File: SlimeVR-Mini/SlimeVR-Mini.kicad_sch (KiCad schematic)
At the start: 1 part, among them U1 ESP32-C3-MINI-1-N4

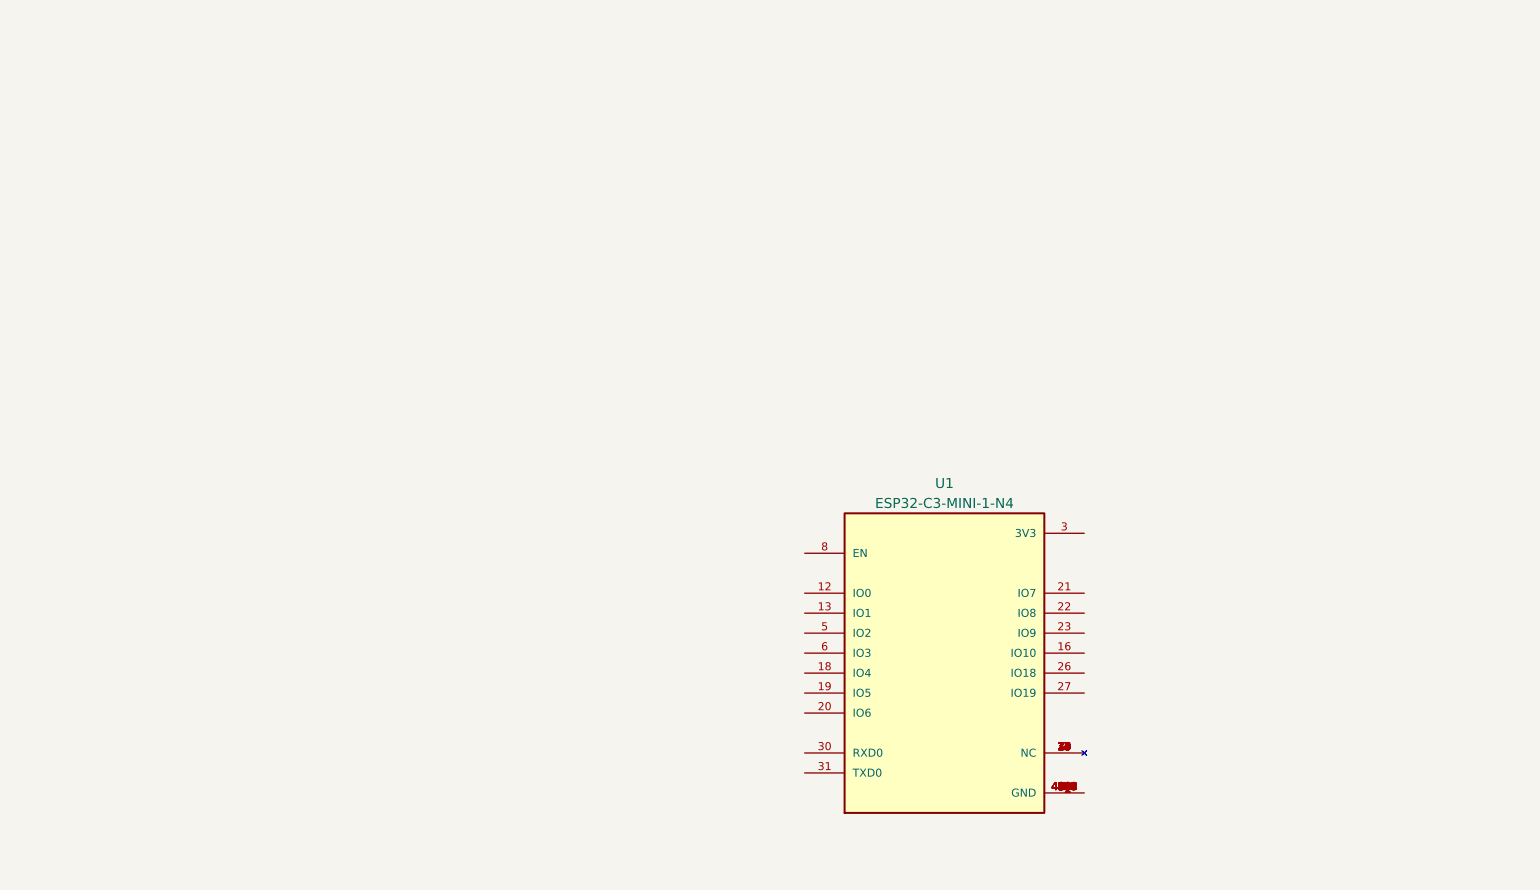
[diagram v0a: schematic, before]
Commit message: basic sheet hierarchy + schematic todo list
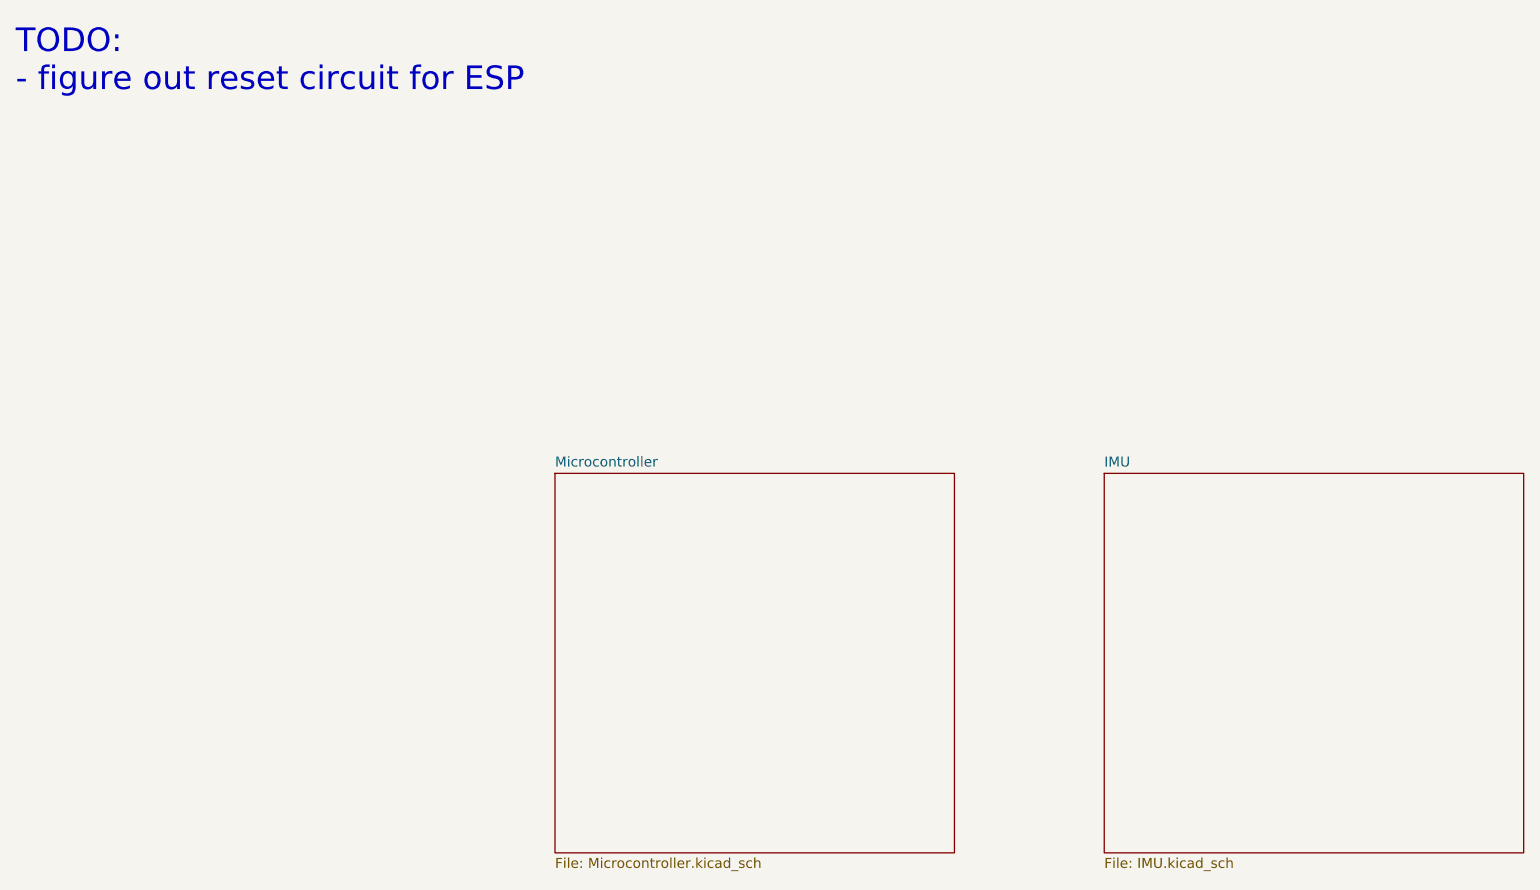
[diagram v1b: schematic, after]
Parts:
- removed U1: ESP32-C3-MINI-1-N4, Project Library:XCVR_ESP32-C3-MINI-1-N4, symbol Project Library:ESP32-C3-MINI-1-N4
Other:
- added sheet IMU (IMU.kicad_sch)
- added sheet Microcontroller (Microcontroller.kicad_sch)
- note added: "TODO: - figure out reset circuit for ESP"
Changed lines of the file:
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@@
 (kicad_sch (version 20230121) (generator eeschema)
   (paper "A4")
-  (symbol (lib_id "Project Library:ESP32-C3-MINI-1-N4") (at 132.08 95.25 0) (unit 1)
-    (in_bom yes) (on_board yes) (dnp no) (fields_autoplaced)
-    (property "Reference" "U1" (at 132.08 73.66 0)
-      (effects (font (size 1.27 1.27)))
+  (text "TODO:\n- figure out reset circuit for ESP\n" (at 13.97 24.13 0)
+    (effects (font (size 3 3)) (justify left bottom))
+  )
+  (sheet (at 152.4 72.39) (size 53.34 48.26) (fields_autoplaced)
+    (stroke (width 0.1524) (type solid))
+    (fill (color 0 0 0 0.0000))
+    (property "Sheetname" "IMU" (at 152.4 71.6784 0)
+      (effects (font (size 1.27 1.27)) (justify left bottom))
     )
-    (property "Value" "ESP32-C3-MINI-1-N4" (at 132.08 76.2 0)
-      (effects (font (size 1.27 1.27)))
+    (property "Sheetfile" "IMU.kicad_sch" (at 152.4 121.2346 0)
+      (effects (font (size 1.27 1.27)) (justify left top))
     )
-    (property "Footprint" "Project Library:XCVR_ESP32-C3-MINI-1-N4" (at 132.08 95.25 0)
-      (effects (font (size 1.27 1.27)) (justify bottom) hide)
-    )
-    (property "Datasheet" "https://www.espressif.com/sites/default/files/documentation/esp32-c3-mini-1_datasheet_en.pdf" (at 132.08 120.65 0)
-      (effects (font (size 1.27 1.27)) hide)
-    )
-    (property "MF" "Espressif Systems" (at 132.08 95.25 0)
-      (effects (font (size 1.27 1.27)) (justify bottom) hide)
-    )
-    (property "MAXIMUM_PACKAGE_HEIGHT" "2.55mm" (at 132.08 95.25 0)
-      (effects (font (size 1.27 1.27)) (justify bottom) hide)
-    )
-    (property "Package" "SMD-53 Espressif Systems" (at 132.08 95.25 0)
-      (effects (font (size 1.27 1.27)) (justify bottom) hide)
-    )
-    (property "PARTREV" "v1.0" (at 132.08 95.25 0)
-      (effects (font (size 1.27 1.27)) (justify bottom) hide)
-    )
-    (property "MP" "ESP32-C3-MINI-1-N4" (at 132.08 95.25 0)
-      (effects (font (size 1.27 1.27)) (justify bottom) hide)
-    )
-    (property "MANUFACTURER" "Espressif Systems" (at 132.08 95.25 0)
-      (effects (font (size 1.27 1.27)) (justify bottom) hide)
-    )
-    (pin "1")
-    (pin "10")
-    (pin "11")
-    (pin "12")
-    (pin "13")
-    (pin "14")
-    (pin "15")
-    (pin "16")
-    (pin "17")
-    (pin "18")
-    (pin "19")
-    (pin "2")
-    (pin "20")
-    (pin "21")
-    (pin "22")
-    (pin "23")
-    (pin "24")
-    (pin "25")
-    (pin "26")
-    (pin "27")
-    (pin "28")
-    (pin "29")
-    (pin "3")
-    (pin "30")
-    (pin "31")
-    (pin "32")
-    (pin "33")
-    (pin "34")
-    (pin "35")
-    (pin "36")
-    (pin "37")
-    (pin "38")
-    (pin "39")
-    (pin "4")
-    (pin "40")
-    (pin "41")
-    (pin "42")
-    (pin "43")
-    (pin "44")
-    (pin "45")
-    (pin "46")
-    (pin "47")
-    (pin "48")
-    (pin "49_1")
-    (pin "49_2")
-    (pin "49_3")
-    (pin "49_4")
-    (pin "49_5")
-    (pin "49_6")
-    (pin "49_7")
-    (pin "49_8")
-    (pin "49_9")
-    (pin "5")
-    (pin "50")
-    (pin "51")
-    (pin "52")
-    (pin "53")
-    (pin "6")
-    (pin "7")
-    (pin "8")
-    (pin "9")
     (instances
       (project "SlimeVR-Mini"
-        (path "/01f70e2f-47c6-495b-b6f7-eee456c9fb57"
-          (reference "U1") (unit 1)
-        )
+        (path "/01f70e2f-47c6-495b-b6f7-eee456c9fb57" (page "3"))
       )
     )
+  )
+  (sheet (at 82.55 72.39) (size 50.8 48.26) (fields_autoplaced)
+    (stroke (width 0.1524) (type solid))
+    (fill (color 0 0 0 0.0000))
+    (property "Sheetname" "Microcontroller" (at 82.55 71.6784 0)
+      (effects (font (size 1.27 1.27)) (justify left bottom))
+    )
+    (property "Sheetfile" "Microcontroller.kicad_sch" (at 82.55 121.2346 0)
+      (effects (font (size 1.27 1.27)) (justify left top))
+    )
+    (instances
+      (project "SlimeVR-Mini"
+        (path "/01f70e2f-47c6-495b-b6f7-eee456c9fb57" (page "2"))
+      )
+    )

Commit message: IMU wiring done-ish
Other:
- sheet IMU ports: added SCL, SDA; removed none
- sheet Microcontroller ports: added SCL, SDA; removed none
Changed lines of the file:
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@@
     (effects (font (size 3 3)) (justify left bottom))
   )
-  (sheet (at 152.4 72.39) (size 53.34 48.26) (fields_autoplaced)
+  (sheet (at 152.4 95.25) (size 17.78 12.7) (fields_autoplaced)
     (stroke (width 0.1524) (type solid))
     (fill (color 0 0 0 0.0000))
-    (property "Sheetname" "IMU" (at 152.4 71.6784 0)
+    (property "Sheetname" "IMU" (at 152.4 94.5384 0)
       (effects (font (size 1.27 1.27)) (justify left bottom))
     )
-    (property "Sheetfile" "IMU.kicad_sch" (at 152.4 121.2346 0)
+    (property "Sheetfile" "IMU.kicad_sch" (at 152.4 108.5346 0)
       (effects (font (size 1.27 1.27)) (justify left top))
+    )
+    (pin "SDA" input (at 152.4 100.33 180)
+      (effects (font (size 1.27 1.27)) (justify left))
+    )
+    (pin "SCL" input (at 152.4 102.87 180)
+      (effects (font (size 1.27 1.27)) (justify left))
     )
     (instances
@@
     )
   )
-  (sheet (at 82.55 72.39) (size 50.8 48.26) (fields_autoplaced)
+  (sheet (at 109.22 90.17) (size 27.94 25.4) (fields_autoplaced)
     (stroke (width 0.1524) (type solid))
     (fill (color 0 0 0 0.0000))
-    (property "Sheetname" "Microcontroller" (at 82.55 71.6784 0)
+    (property "Sheetname" "Microcontroller" (at 109.22 89.4584 0)
       (effects (font (size 1.27 1.27)) (justify left bottom))
     )
-    (property "Sheetfile" "Microcontroller.kicad_sch" (at 82.55 121.2346 0)
+    (property "Sheetfile" "Microcontroller.kicad_sch" (at 109.22 116.1546 0)
       (effects (font (size 1.27 1.27)) (justify left top))
     )
+    (pin "SDA" input (at 137.16 100.33 0)
+      (effects (font (size 1.27 1.27)) (justify right))
+    )
+    (pin "SCL" input (at 137.16 102.87 0)
+      (effects (font (size 1.27 1.27)) (justify right))
+    )
     (instances

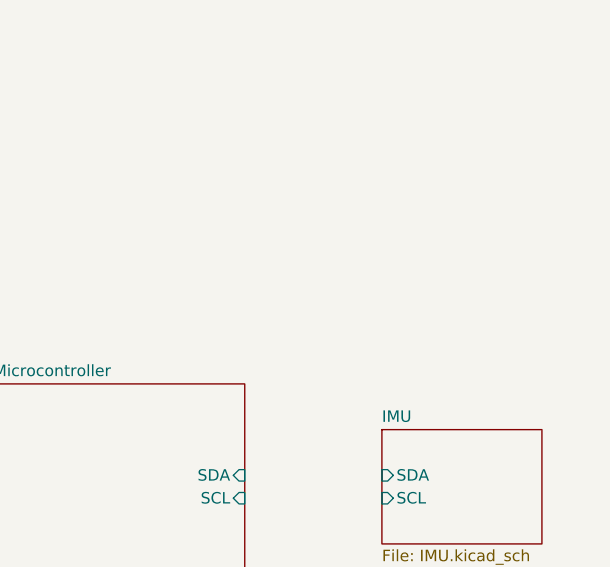
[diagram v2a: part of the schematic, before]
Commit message: added Power page + fixing symbols and footprints
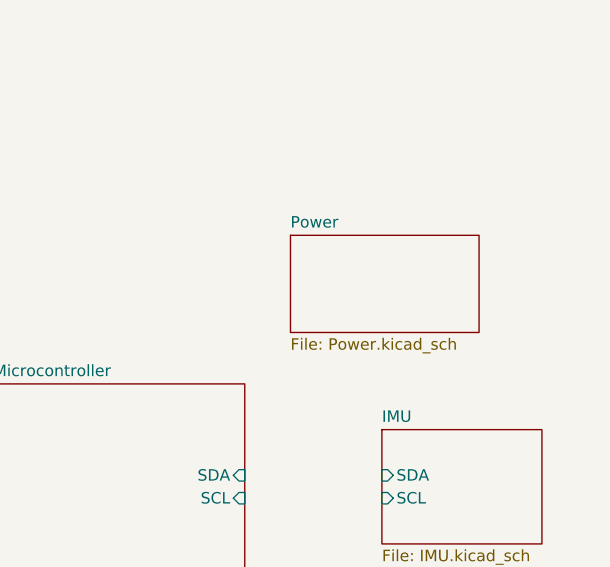
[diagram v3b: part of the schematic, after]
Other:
- added sheet Power (Power.kicad_sch)
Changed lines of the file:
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@@
+    )
+  )
+  (sheet (at 142.24 73.66) (size 20.955 10.795) (fields_autoplaced)
+    (stroke (width 0.1524) (type solid))
+    (fill (color 0 0 0 0.0000))
+    (property "Sheetname" "Power" (at 142.24 72.9484 0)
+      (effects (font (size 1.27 1.27)) (justify left bottom))
+    )
+    (property "Sheetfile" "Power.kicad_sch" (at 142.24 85.0396 0)
+      (effects (font (size 1.27 1.27)) (justify left top))
+    )
+    (instances
+      (project "SlimeVR-Mini"
+        (path "/01f70e2f-47c6-495b-b6f7-eee456c9fb57" (page "4"))
+      )
     )
   )
